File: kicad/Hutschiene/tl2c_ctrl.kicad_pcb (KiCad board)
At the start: 4 copper layers, 62.2 x 58.4 mm, 72 parts, among them IC101 ATTINY20-X, P101 12VDC, P102 I2C Master, P103 Spare, P104 TPI Header, P105 LED_DRIVER, P109 5VDC, P201 Mode_Bridge, P301 CONN_PIR_OG, P302 CONN_PIR_EG, P303 CONN_PIR_UG, Q301 IRLML2502, Q302 IRLML2502, Q303 IRLML2502, SW101 TL3315NF160Q, U201 LF120ABDT-TR, U202 TPS70933

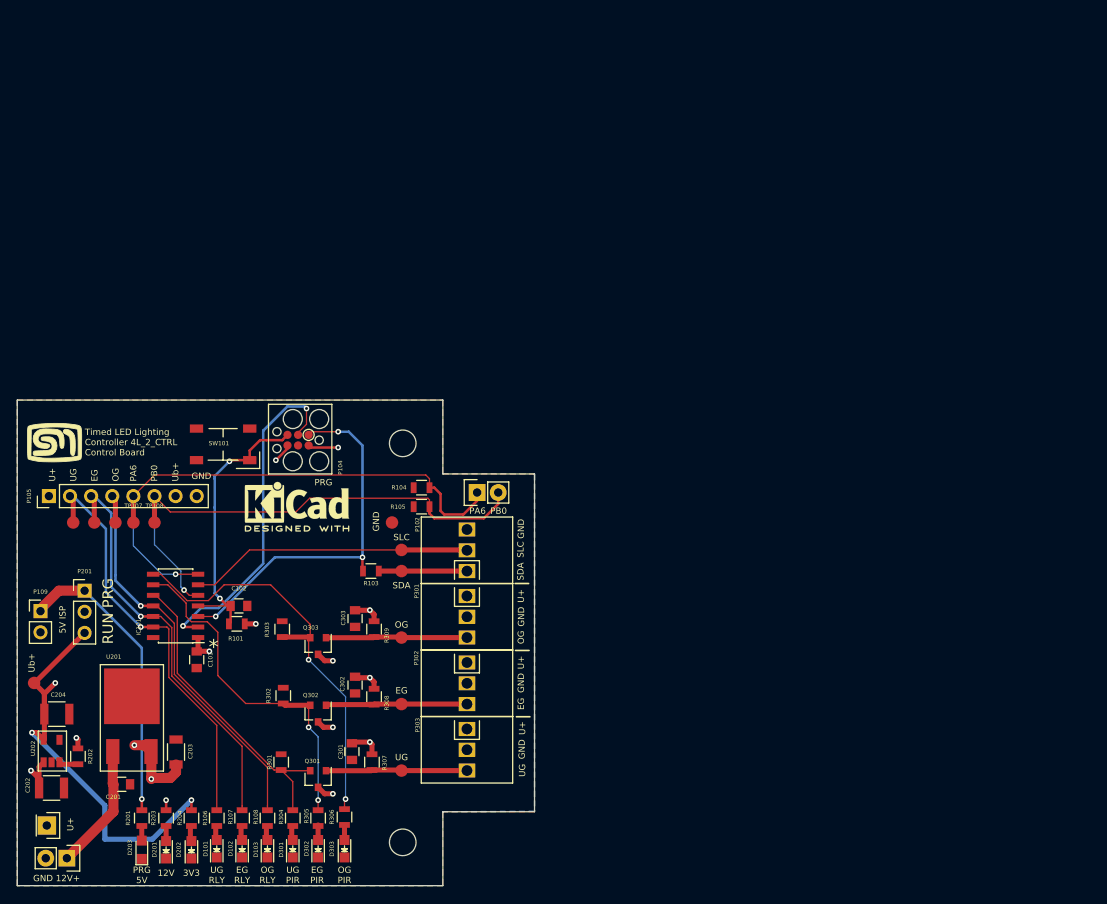
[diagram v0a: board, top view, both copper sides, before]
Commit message: Adjusted the size and location of the terminal blocks
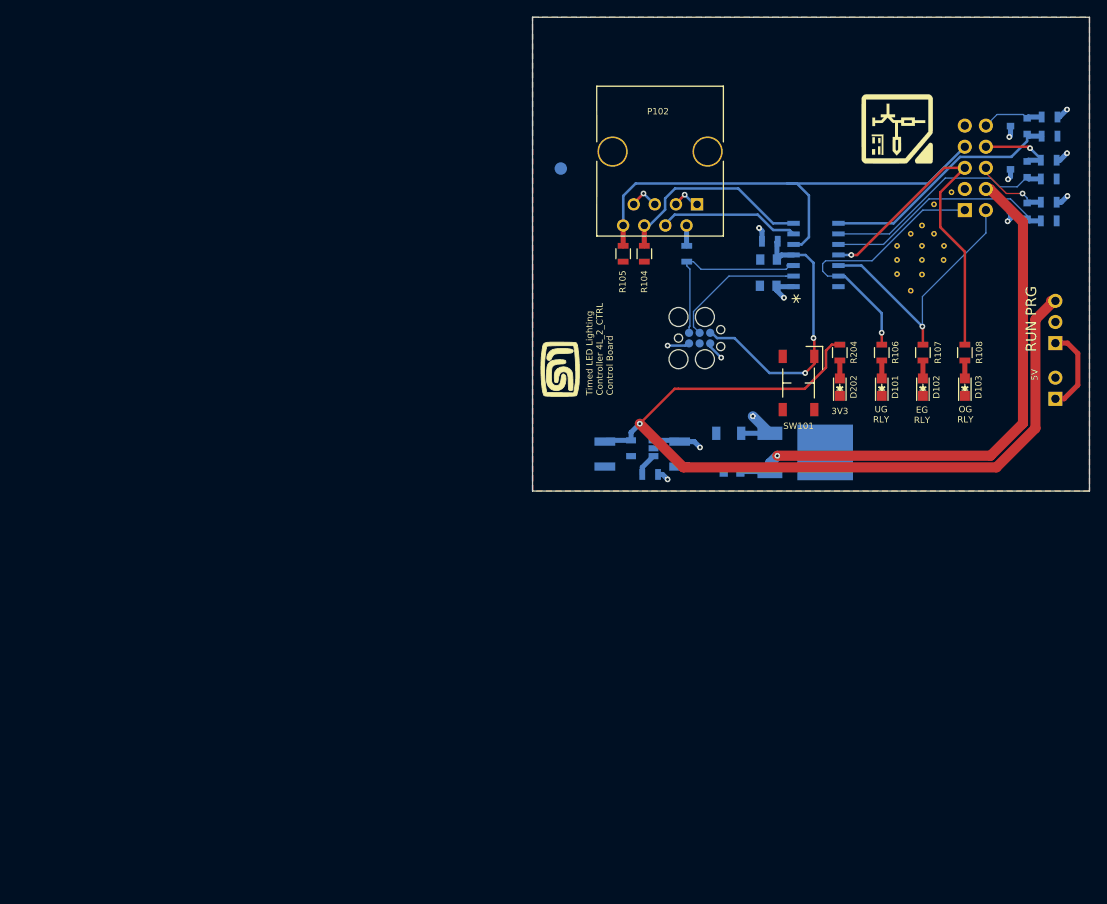
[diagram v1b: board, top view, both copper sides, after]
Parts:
- removed C301, C302, C303: 100nF 50V, Capacitors_SMD:C_0805
- removed D201: 12VDC, LEDs:LED_0805
- removed D203: 5VDC, LEDs:LED_0805
- removed D301: LED__SIG_UG, LEDs:LED_0805
- removed D302: LED__SIG_EG, LEDs:LED_0805
- removed D303: LED__SIG_OG, LEDs:LED_0805
- removed the G*** at (97.2, 125.7)
- removed P101: 12VDC, Pin_Headers:Pin_Header_Straight_1x02
- removed P105: LED_DRIVER, Pin_Headers:Pin_Header_Straight_1x08_Pitch2.54mm
- removed P301: CONN_PIR_OG, tl2c-footprint:Spring_Terminal_Block_1_x_3
- removed P302: CONN_PIR_EG, tl2c-footprint:Spring_Terminal_Block_1_x_3
- removed P303: CONN_PIR_UG, tl2c-footprint:Spring_Terminal_Block_1_x_3
- removed R201, R304, R305, R306: 660Ω, Resistors_SMD:R_0805
- removed R203: 2k4Ω, Resistors_SMD:R_0805
- removed the REF** at (139.1, 125.9)
- removed the REF** at (139.1, 173.9)
- removed REF***: KiCad-Logo2_6mm_SilkScreen, Symbols:KiCad-Logo2_6mm_SilkScreen
- removed TP102: TPSCL, Measurement_Points:Measurement_Point_Round-SMD-Pad_Small
- removed TP103: TPSDA, Measurement_Points:Measurement_Point_Round-SMD-Pad_Small
- removed TP104: TP_RLY_UG, Measurement_Points:Measurement_Point_Round-SMD-Pad_Small
- removed TP105: TP_RLY_EG, Measurement_Points:Measurement_Point_Round-SMD-Pad_Small
- removed TP106: TP_RLY_OG, Measurement_Points:Measurement_Point_Round-SMD-Pad_Small
- removed TP107: PA6, Measurement_Points:Measurement_Point_Round-SMD-Pad_Small
- removed TP108: PB0, Measurement_Points:Measurement_Point_Round-SMD-Pad_Small
- removed TP201: TP3V3, Measurement_Points:Measurement_Point_Round-SMD-Pad_Small
- removed TP202: TP12V, Pin_Headers:Pin_Header_Straight_1x01
- removed TP301: TP_UG, Measurement_Points:Measurement_Point_Round-SMD-Pad_Small
- removed TP302, TP303: TP_EG, Measurement_Points:Measurement_Point_Round-SMD-Pad_Small
- added G***: LOGO, tl2c-footprint:MyBasic_rounded_50_1, F.Cu at (158.0, 117.0)
- added G***: LOGO, tl2c-footprint:KiCad_LOGO_9mm, F.Cu at (198.7, 88.0)
- added G***: LOGO, tl2c-footprint:MyBasic_rounded_50_1, B.Cu at (160.0, 77.8)
- added G***: LOGO, tl2c-footprint:KiCad_LOGO_9mm, B.Cu at (208.0, 122.4)
- added REF**: Stitch_VIA, tl2c-footprint:Stitch_VIA, F.Cu at (200.2, 100.7)
- added REF**: Stitch_VIA, tl2c-footprint:Stitch_VIA, F.Cu at (201.6, 99.7)
- added REF**11: Stitch_VIA, tl2c-footprint:Stitch_VIA, F.Cu at (198.6, 102.1)
- added REF**12: Stitch_VIA, tl2c-footprint:Stitch_VIA, F.Cu at (198.6, 103.8)
- added REF**13: Stitch_VIA, tl2c-footprint:Stitch_VIA, F.Cu at (200.2, 107.5)
- added REF**21: Stitch_VIA, tl2c-footprint:Stitch_VIA, F.Cu at (198.6, 105.5)
- added REF**22: Stitch_VIA, tl2c-footprint:Stitch_VIA, F.Cu at (201.6, 103.8)
- added REF**31: Stitch_VIA, tl2c-footprint:Stitch_VIA, F.Cu at (205.1, 95.7)
- added REF**31: Stitch_VIA, tl2c-footprint:Stitch_VIA, F.Cu at (203.0, 97.1)
- added REF**31: Stitch_VIA, tl2c-footprint:Stitch_VIA, F.Cu at (203.0, 100.7)
- added REF**31: Stitch_VIA, tl2c-footprint:Stitch_VIA, F.Cu at (201.6, 102.1)
- added REF**32: Stitch_VIA, tl2c-footprint:Stitch_VIA, F.Cu at (204.2, 102.1)
- added REF**41: Stitch_VIA, tl2c-footprint:Stitch_VIA, F.Cu at (204.2, 103.8)
- added REF**42: Stitch_VIA, tl2c-footprint:Stitch_VIA, F.Cu at (201.6, 105.5)
- C101, C102, C201, C202, C203, C204, IC101, P104, P109, P201, Q301, Q302, Q303, R101, R103, R202, R301, R302, R303, R307, R308, R309, TP101, U201, U202: moved to B.Cu
- P102: value I2C Master -> RJ45; footprint tl2c-footprint:Spring_Terminal_Block_1_x_3 -> tl2c-footprint:RJ45_8P8C
- P103: value Spare -> CTL CONN; footprint Pin_Headers:Pin_Header_Straight_1x02 -> Pin_Headers:Pin_Header_Straight_2x05_Pitch2.54mm; moved to B.Cu
- moved P109 124.7 mm to (217.6, 120.5)
- moved P201 120.5 mm to (217.6, 113.8)
- moved R301 113.0 mm to (216.8, 99.1), turned to 180 degrees
- moved R302 111.1 mm to (216.8, 94.0), turned to 180 degrees
- moved R303 109.7 mm to (216.9, 88.9), turned to 180 degrees
- moved Q301 108.5 mm to (213.2, 97.9), turned to 180 degrees
- moved Q302 106.7 mm to (213.2, 92.9), turned to 180 degrees
- moved R307 105.7 mm to (216.8, 96.8), turned to 0 degrees
- moved Q303 105.0 mm to (213.2, 87.7), turned to 180 degrees
- moved R308 103.7 mm to (216.8, 91.8), turned to 0 degrees
- moved R309 102.0 mm to (216.9, 86.6), turned to 0 degrees
- moved R108 100.9 mm to (206.7, 114.9)
- moved D103 100.6 mm to (206.7, 119.1)
- moved R107 99.2 mm to (201.7, 114.9)
- moved D102 98.9 mm to (201.7, 119.1)
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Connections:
- IC101 pad 7: /GPIO_PA6 -> /RLY_INT
- P102 pad 1: /SDA -> GND
- P102 pad 2: /SCL -> /SDA
- P103 pad 1: /GPIO_PA6 -> /RelayUG
- P103 pad 2: /GPIO_PB2 -> /RelayEG
- P104 pad 4: Net-(P104-Pad4) -> (no net)
- R104 pad 2: /GPIO_PA6 -> /RLY_INT
- SW101 pad 2: Net-(SW101-Pad2) -> (no net)
- SW101 pad 4: Net-(SW101-Pad4) -> (no net)
- U202 pad 4: Net-(U202-Pad4) -> (no net)
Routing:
- net /GPIO_PA6: track 67.9 -> 0.00 mm, vias 1 -> 0
- net /Power System/U+In: track 15.2 -> 67.8 mm, vias 0 -> 1
- net Net-(C204-Pad1): track 52.2 -> 103.7 mm, vias 3 -> 1
- net /Power System/5V: track 35.7 -> 10.4 mm, vias 1 -> 0
- net /RLY_INT: track 0.00 -> 24.8 mm
- net /TPICLK: track 40.9 -> 16.7 mm, vias 2 -> 0
- net /TPIDATA: track 45.8 -> 22.8 mm, vias 3 -> 0
- net /PIR13/SIG_OG: track 50.6 -> 29.5 mm, vias 2 -> 0
- net /RelayEG: track 50.2 -> 32.9 mm
- net /SCL: track 34.1 -> 17.0 mm
- net /RelayUG: track 50.5 -> 33.8 mm
- net /PIR13/SIG_EG: track 42.2 -> 28.1 mm, vias 2 -> 0
- net /PIR13/U+: track 29.0 -> 18.6 mm, vias 8 -> 6
- net /PIR13/SIG_UG: track 38.1 -> 28.0 mm
- net /PIR13/PIR_OG: track 17.0 -> 7.51 mm
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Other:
- board size 62.2 x 58.4 mm -> 67 x 57 mm
- board text added: "5V"
- board text added: "ISP PWR"
- board text removed: "12V"
- board text removed: "5V ISP"
- board text removed: "EG"
- board text removed: "EG PIR"
- board text removed: "GND"
- board text removed: "GND 12V+"
- board text removed: "OG"
- board text removed: "OG PIR"
- board text removed: "PA6"
- board text removed: "PB0"
- board text removed: "PRG"
- board text removed: "PRG 5V"
- board text removed: "SDA"
- board text removed: "SLC"
- board text removed: "U+"
- board text removed: "UG"
- board text removed: "UG PIR"
- board text removed: "Ub+"

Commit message: Pushed the boards to OSHPark
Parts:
- moved G*** 18.6 mm to (215.4, 79.9), turned to 0 degrees
- moved G*** 6.96 mm to (163.4, 121.4), turned to 0 degrees
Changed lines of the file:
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@@
     (links 98)
     (no_connects 0)
-    (area 20.250001 40.4 248.26 176.820001)
+    (area 136.020001 61.85 248.26 140.800001)
     (thickness 1.6)
     (drawings 38)
@@
     (40 Dwgs.User user)
     (41 Cmts.User user)
-    (42 Eco1.User user)
-    (43 Eco2.User user)
+    (42 Eco1.User user hide)
+    (43 Eco2.User user hide)
     (44 Edge.Cuts user)
     (45 Margin user)
@@
     (tags "capacitor 0805")
     (attr smd)
-    (fp_text reference C201 (at -1.016 -1.524 180) (layer B.SilkS)
+    (fp_text reference C201 (at -0.01 1.65 180) (layer B.SilkS)
       (effects (font (size 0.762 0.762) (thickness 0.127)) (justify mirror))
     )
@@
     (tags "resistor 0805")
     (attr smd)
-    (fp_text reference R202 (at -0.0127 -1.4859) (layer B.SilkS)
+    (fp_text reference R202 (at -3.38 0.66) (layer B.SilkS)
       (effects (font (size 0.762 0.762) (thickness 0.127)) (justify mirror))
     )
@@
   )
   (module tl2c-footprint:MyBasic_rounded_50_1 locked (layer F.Cu)
-    (at 157.98 116.99 90)
-    (fp_text reference G*** (at 0 0 90) (layer F.SilkS) hide
+    (at 163.37 121.4)
+    (fp_text reference G*** (at 0 0) (layer F.SilkS) hide
       (effects (font (thickness 0.3)))
     )
-    (fp_text value LOGO (at 0.75 0 90) (layer F.SilkS) hide
+    (fp_text value LOGO (at 0.75 0) (layer F.SilkS) hide
       (effects (font (thickness 0.3)))
     )
@@
   )
   (module tl2c-footprint:KiCad_LOGO_9mm (layer F.Cu)
-    (at 198.68 88.01 270)
-    (fp_text reference G*** (at 0 6.5 270) (layer F.SilkS) hide
+    (at 215.4 79.92)
+    (fp_text reference G*** (at 0 6.5) (layer F.SilkS) hide
       (effects (font (thickness 0.3)))
     )
-    (fp_text value LOGO (at 0 -6 270) (layer F.SilkS) hide
+    (fp_text value LOGO (at 0 -6) (layer F.SilkS) hide
       (effects (font (thickness 0.3)))
     )
@@
       (xy 1.195199 -0.12652) (xy 1.195199 -0.12652)) (layer B.SilkS) (width 0.1))
   )
-  (module tl2c-footprint:KiCad_LOGO_9mm locked (layer B.Cu)
+  (module tl2c-footprint:KiCad_LOGO_9mm (layer B.Cu)
     (at 208.03 122.43 180)
     (fp_text reference G*** (at 0 -6.5 180) (layer B.SilkS) hide
@@
   (gr_line (start 221.7 74.6) (end 221.7 131.6) (angle 90) (layer Edge.Cuts) (width 0.15))
   (gr_line (start 154.7 74.6) (end 221.7 74.6) (angle 90) (layer Edge.Cuts) (width 0.15))
-  (gr_text "ISP \nPWR" (at 157.8 95.5 90) (layer B.SilkS)
+  (gr_text "ISP \nPWR" (at 220.31 119.16 90) (layer B.SilkS)
     (effects (font (size 0.762 0.762) (thickness 0.127)) (justify mirror))
   )
-  (gr_text "RUN PRG" (at 214.7 110.9 90) (layer F.SilkS)
-    (effects (font (size 1.27 1.27) (thickness 0.127)))
-  )
-  (gr_text 5V (at 215.1 117.6 90) (layer F.SilkS)
-    (effects (font (size 0.762 0.762) (thickness 0.127)))
-  )
-  (gr_text * (at 186.85 108.45 90) (layer F.SilkS)
-    (effects (font (size 1.778 1.778) (thickness 0.254)))
+  (gr_text "RUN PRG" (at 214.88 111.4 90) (layer B.SilkS)
+    (effects (font (size 1.27 1.27) (thickness 0.127)) (justify mirror))
+  )
+  (gr_text 5V (at 215.47 120.48 90) (layer B.SilkS)
+    (effects (font (size 0.762 0.762) (thickness 0.127)) (justify mirror))
+  )
+  (gr_text * (at 186.82 108.47 90) (layer B.SilkS)
+    (effects (font (size 1.778 1.778) (thickness 0.254)) (justify mirror))
   )
   (gr_text "OG\nRLY" (at 206.77 122.38) (layer F.SilkS)
@@
     (effects (font (size 0.762 0.762) (thickness 0.127)))
   )
-  (gr_text "Timed LED Lighting \nController 4L_2_CTRL\nControl Board" (at 162.78 120.1 90) (layer F.SilkS)
+  (gr_text "Timed LED Lighting \nController 4L_2_CTRL\nControl Board" (at 167.58 121.44) (layer F.SilkS)
     (effects (font (size 0.762 0.762) (thickness 0.127)) (justify left))
   )

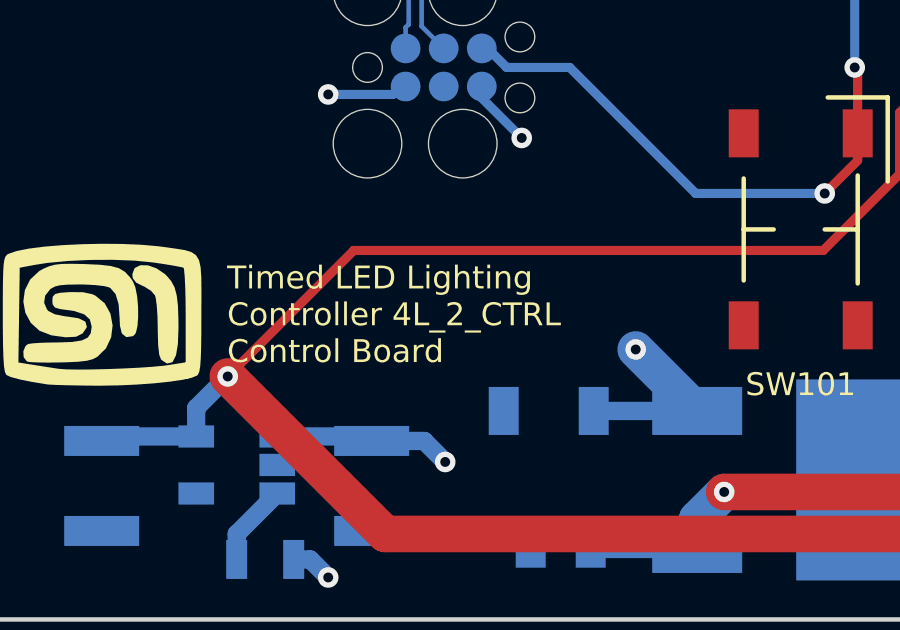
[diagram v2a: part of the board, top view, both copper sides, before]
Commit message: Corrections to the terminal block drill holes
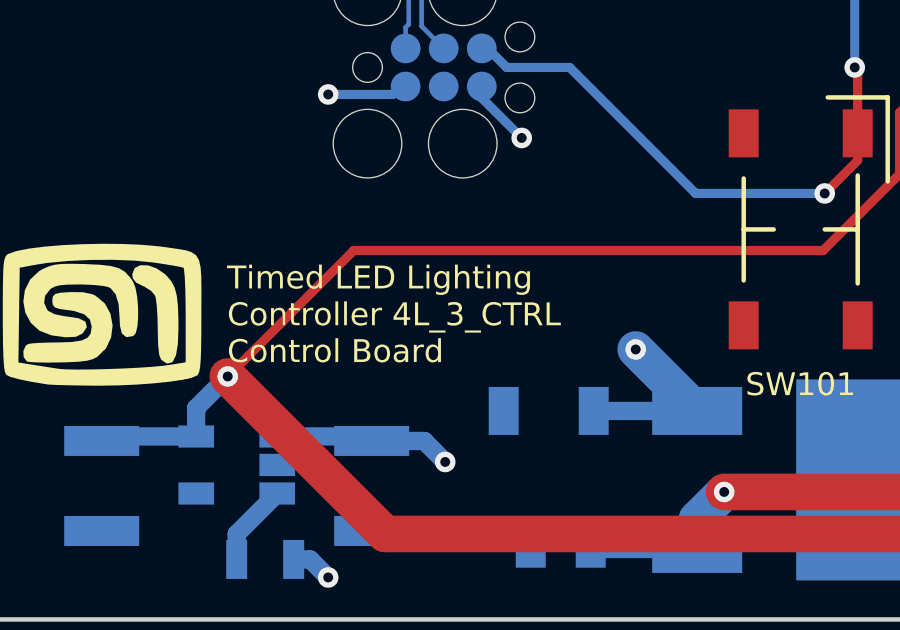
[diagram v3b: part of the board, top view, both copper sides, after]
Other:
- board text added: "Timed LED Lighting Controller 4L_3_CTRL Control Board"
- board text removed: "Timed LED Lighting Controller 4L_2_CTRL Control Board"
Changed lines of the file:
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@@
   (page A4)
   (title_block
-    (title "Timed LED Lighting Controller - Master Layout")
-    (rev 4L_2H)
+    (title "Timed LED Lighting Controller - Control board layout")
+    (rev 4L_3_CRL)
   )
   (layers
@@
     (arrow2b (pts (xy 240.26 74.6) (xy 240.846421 75.726504)))
   )
-  (gr_text "Timed LED Lighting \nController 4L_2_CTRL\nControl Board" (at 164.59 77.53 180) (layer B.SilkS)
+  (gr_text "Timed LED Lighting \nController 4L_3_CTRL\nControl Board" (at 164.59 77.53 180) (layer B.SilkS)
     (effects (font (size 0.762 0.762) (thickness 0.127)) (justify left mirror))
   )
@@
     (effects (font (size 0.762 0.762) (thickness 0.127)))
   )
-  (gr_text "Timed LED Lighting \nController 4L_2_CTRL\nControl Board" (at 167.58 121.44) (layer F.SilkS)
+  (gr_text "Timed LED Lighting \nController 4L_3_CTRL\nControl Board" (at 167.58 121.44) (layer F.SilkS)
     (effects (font (size 0.762 0.762) (thickness 0.127)) (justify left))
   )

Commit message: Correction to the board connected and seperated out the pwr
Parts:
- removed the G*** at (160.0, 77.8)
- removed the G*** at (208.0, 122.4)
- removed REF** (x2), REF**11, REF**12, REF**13, REF**21, REF**22, REF**32, REF**41, REF**42: Stitch_VIA, tl2c-footprint:Stitch_VIA
- removed the REF**31 at (203.0, 100.7)
- removed the REF**31 at (201.6, 102.1)
- added P107: CTL PWR, Pin_Headers:Pin_Header_Straight_1x02_Pitch2.54mm, B.Cu at (208.8, 79.9)
- added REF**31: Stitch_VIA, tl2c-footprint:Stitch_VIA, F.Cu at (195.8, 102.5)
- added REF**31: Stitch_VIA, tl2c-footprint:Stitch_VIA, F.Cu at (204.2, 98.5)
- added REF**31: Stitch_VIA, tl2c-footprint:Stitch_VIA, F.Cu at (201.9, 98.5)
- added REF**31: Stitch_VIA, tl2c-footprint:Stitch_VIA, F.Cu at (200.6, 99.8)
- added REF**31: Stitch_VIA, tl2c-footprint:Stitch_VIA, F.Cu at (207.9, 92.0)
- added REF**31: Stitch_VIA, tl2c-footprint:Stitch_VIA, F.Cu at (207.9, 94.6)
- added REF**31: Stitch_VIA, tl2c-footprint:Stitch_VIA, F.Cu at (196.7, 101.3)
- added REF**31: Stitch_VIA, tl2c-footprint:Stitch_VIA, F.Cu at (194.3, 101.3)
- added REF**31: Stitch_VIA, tl2c-footprint:Stitch_VIA, F.Cu at (195.4, 100.0)
- added REF**31: Stitch_VIA, tl2c-footprint:Stitch_VIA, F.Cu at (193.4, 100.0)
- added REF**31: Stitch_VIA, tl2c-footprint:Stitch_VIA, F.Cu at (194.5, 98.6)
- added REF**31: Stitch_VIA, tl2c-footprint:Stitch_VIA, F.Cu at (196.9, 98.6)
- added REF**31: Stitch_VIA, tl2c-footprint:Stitch_VIA, F.Cu at (205.1, 99.8)
- added REF**31: Stitch_VIA, tl2c-footprint:Stitch_VIA, F.Cu at (202.8, 99.8)
- C204: footprint Capacitors_SMD:C_1210 -> Capacitors_SMD:C_1206
- P102, R104, R105: moved to B.Cu
- P104: footprint tl2c-footprint:TC2030-IDC-FP_ISP_Connector -> Connect:Tag-Connect_TC2030-IDC-NL; moved to F.Cu
- P109, P201: moved to F.Cu
- SW101: footprint tl2c-footprint:PTS525SM15SMTR2LFS -> tl2c-footprint:TACTILE_FSM2JSMAA
- moved P109 60.0 mm to (159.4, 105.6), turned to 180 degrees
- moved P201 58.3 mm to (159.4, 109.7)
- moved C201 56.9 mm to (202.5, 77.6), turned to 0 degrees
- moved C203 49.1 mm to (202.9, 82.2), turned to 0 degrees
- moved U201 47.1 mm to (191.3, 79.9), turned to 0 degrees
- moved R202 46.0 mm to (194.7, 91.5)
- moved C202 46.0 mm to (198.2, 89.1)
- moved C204 46.0 mm to (189.2, 89.1)
- moved U202 46.0 mm to (193.7, 88.4)
- moved G*** 45.9 mm to (216.3, 125.8)
- moved G*** 43.5 mm to (159.2, 78.1)
- moved TP101 35.4 mm to (193.4, 95.2)
- moved P104 20.9 mm to (184.4, 94.7), turned to 90 degrees
- moved P102 10.2 mm to (175.8, 99.6), turned to 0 degrees
- moved R105 10.2 mm to (175.8, 103.1)
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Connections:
- P103 pad 4: /Power System/U+In -> (no net)
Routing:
- net /Power System/U+In: track 67.8 -> 15.7 mm, vias 1 -> 0
- net /GPIO_PB2: track 60.4 -> 43.6 mm, vias 0 -> 2
- net /TPIDATA: track 22.8 -> 34.0 mm, vias 0 -> 1
- net /Power System/5V: track 10.4 -> 4.05 mm
- net Net-(C204-Pad1): track 103.7 -> 98.5 mm, vias 1 -> 0
- net /~Reset: track 34.9 -> 40.1 mm
- net /RelayOG: track 44.0 -> 39.0 mm
- net /TPICLK: track 16.7 -> 19.4 mm, vias 0 -> 1
- net /RLY_INT: track 24.8 -> 22.4 mm, vias 0 -> 1
- net GND: track 9.52 -> 7.25 mm, vias 3 -> 2
- net /RelayUG: track 33.8 -> 32.7 mm
- net /PIR13/Ub+: track 12.7 -> 11.9 mm
- net /RelayEG: track 32.9 -> 32.1 mm
- net /PIR13/U+: track 18.6 -> 19.2 mm
- net /PIR13/PIR_UG: track 9.12 -> 8.53 mm
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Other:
- board text added: "+"
- board text added: "12VDC"
- board text added: "PRG"
- board text added: "Reset"
- board text added: "Timed LED Lighting Controller 4L_4_CTRL Control Board"
- board text removed: "Timed LED Lighting Controller 4L_3_CTRL Control Board"
